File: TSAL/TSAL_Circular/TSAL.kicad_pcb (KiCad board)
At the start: 2 copper layers, 68.6 x 68.6 mm, 49 parts, among them J1 Main Connector, U1 L7805, U2 LM555, U3 SN754410

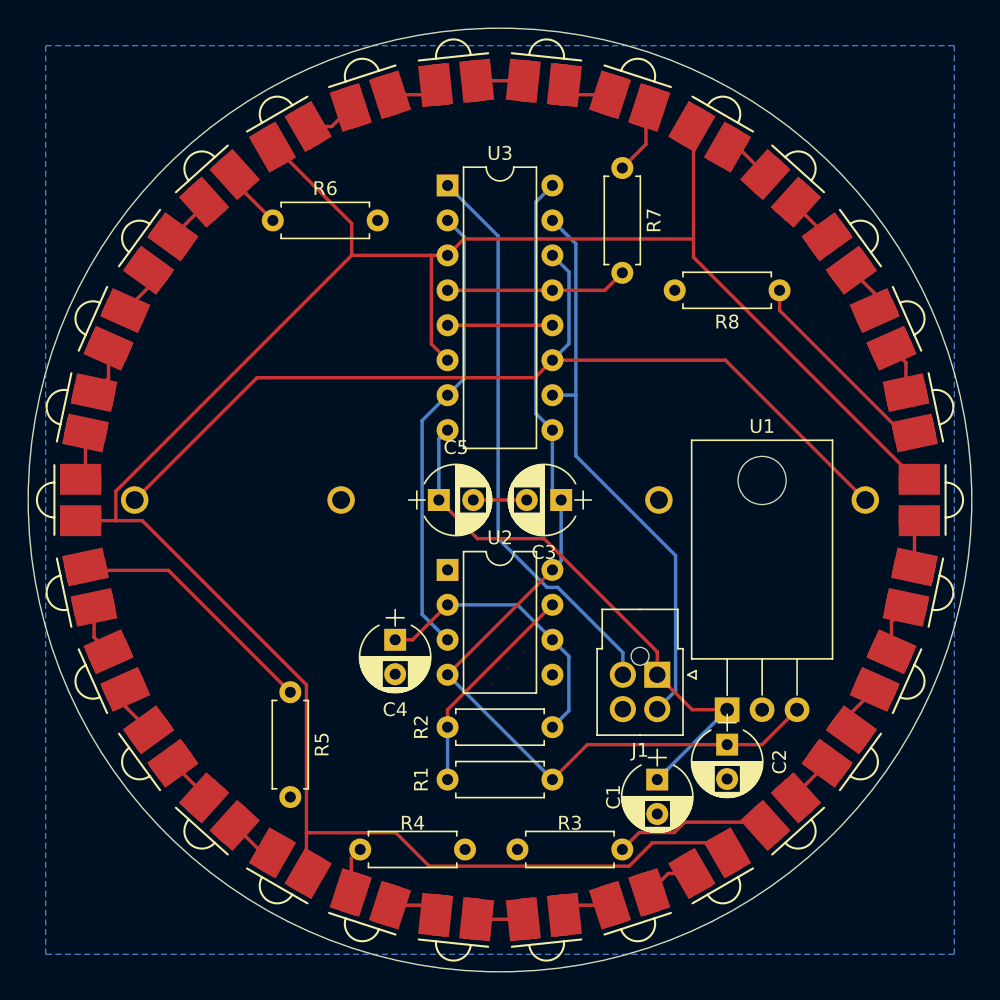
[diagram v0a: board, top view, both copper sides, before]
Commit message: add mounting holes and surface mount resistors to TSAL
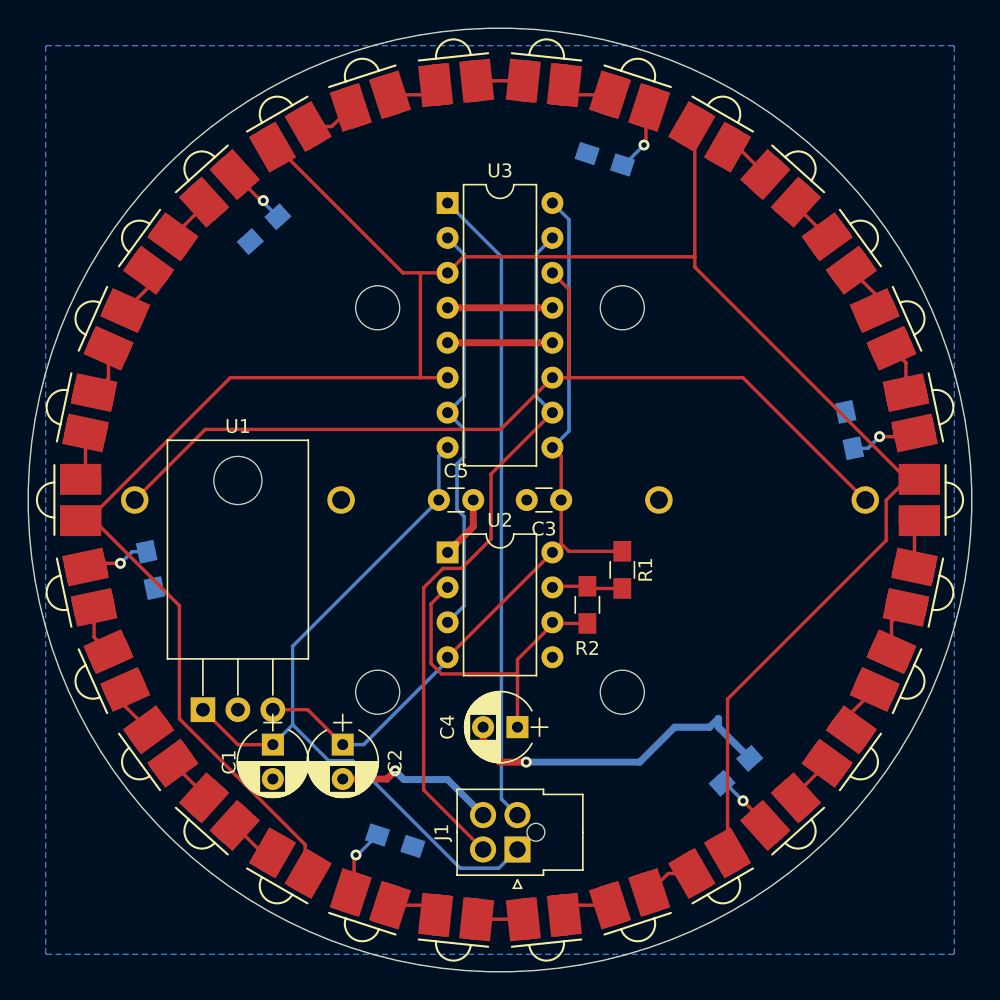
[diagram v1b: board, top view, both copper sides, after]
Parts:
- added H1: MtngHole, Mounting_Holes:MountingHole_3.2mm_M3, F.Cu at (143.5, 87.6)
- added H2: MtngHole, Mounting_Holes:MountingHole_3.2mm_M3, F.Cu at (143.5, 115.6)
- added H3: MtngHole, Mounting_Holes:MountingHole_3.2mm_M3, F.Cu at (161.3, 87.6)
- added H4: MtngHole, Mounting_Holes:MountingHole_3.2mm_M3, F.Cu at (161.3, 115.6)
- C3, C5: footprint Capacitors_THT:CP_Radial_D5.0mm_P2.50mm -> Capacitors_THT:C_Disc_D3.0mm_W1.6mm_P2.50mm
- R1, R2: footprint Resistors_THT:R_Axial_DIN0207_L6.3mm_D2.5mm_P7.62mm_Horizontal -> Resistors_SMD:R_0805_HandSoldering
- R3, R4, R5, R6, R7, R8: footprint Resistors_THT:R_Axial_DIN0207_L6.3mm_D2.5mm_P7.62mm_Horizontal -> Resistors_SMD:R_0805_HandSoldering; moved to B.Cu
- moved U1 38.1 mm to (130.8, 116.8)
- moved C1 28.1 mm to (135.9, 119.4)
- moved C2 27.9 mm to (141.0, 119.4)
- moved J1 16.3 mm to (153.7, 127.0), turned to 90 degrees
- moved R1 16.1 mm to (161.3, 106.7), turned to 270 degrees
- moved R2 13.5 mm to (158.8, 109.2), turned to 270 degrees
- moved R5 13.5 mm to (127.0, 106.7), turned to 282 degrees
- moved R8 11.4 mm to (177.8, 96.5), turned to 102 degrees
- moved C4 10.9 mm to (153.7, 118.1), turned to 180 degrees
- moved R3 10.0 mm to (169.5, 121.3), turned to 42 degrees
- moved R4 2.62 mm to (144.8, 126.4), turned to 342 degrees
- moved R7 1.42 mm to (160.0, 76.8), turned to 162 degrees
- moved U2 1.27 mm to (148.6, 105.4)
- moved U3 1.27 mm to (148.6, 80.0)
- moved R6 0.90 mm to (135.3, 81.9), turned to 222 degrees
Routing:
- net /GND: track 24.7 -> 55.7 mm, vias 0 -> 2
- net Net-(D15-Pad1): track 18.8 -> 5.15 mm, vias 0 -> 1
- net /12V: track 40.8 -> 54.2 mm
- net /5V: track 70.9 -> 58.9 mm
- net Net-(R1-Pad2): track 15.9 -> 5.18 mm
- net /SIG_RTDS: track 41.5 -> 51.9 mm
- net Net-(D30-Pad1): track 15.1 -> 5.15 mm, vias 0 -> 1
- net Net-(D5-Pad1): track 11.6 -> 4.70 mm, vias 0 -> 1
- net /SIG_TSAL: track 41.3 -> 46.6 mm
- net Net-(C4-Pad1): track 20.9 -> 23.8 mm
- net Net-(U2-Pad3): track 33.0 -> 30.3 mm
- net Net-(D10-Pad1): track 3.66 -> 5.26 mm, vias 0 -> 1
- net /RTDS_H: track 70.1 -> 68.6 mm
- net /OSC: track 171.5 -> 172.4 mm
- net Net-(D25-Pad1): track 5.42 -> 5.26 mm, vias 0 -> 1
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
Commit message: hopefully finalize PCBs for send to manufacturing
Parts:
- R3, R4, R5, R6, R7, R8: moved to F.Cu
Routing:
- net /GND: track 55.7 -> 35.7 mm, vias 2 -> 8
- net /RTDS_H: track 68.6 -> 77.3 mm
- net /SIG_TSAL: track 46.6 -> 50.8 mm
- net /SIG_RTDS: track 51.9 -> 48.7 mm
- net /OSC: track 172.4 -> 170.1 mm
- net /5V: track 58.9 -> 59.8 mm
- net /12V: track 54.2 -> 54.7 mm
- net Net-(D20-Pad1): track 4.73 -> 4.66 mm, vias 1 -> 0
- net Net-(D25-Pad1): track 5.26 -> 5.20 mm, vias 1 -> 0
- net Net-(D10-Pad1): track 5.26 -> 5.20 mm, vias 1 -> 0
- net Net-(D5-Pad1): track 4.70 -> 4.66 mm, vias 1 -> 0
- net Net-(D30-Pad1): vias 1 -> 0
- net Net-(D15-Pad1): vias 1 -> 0

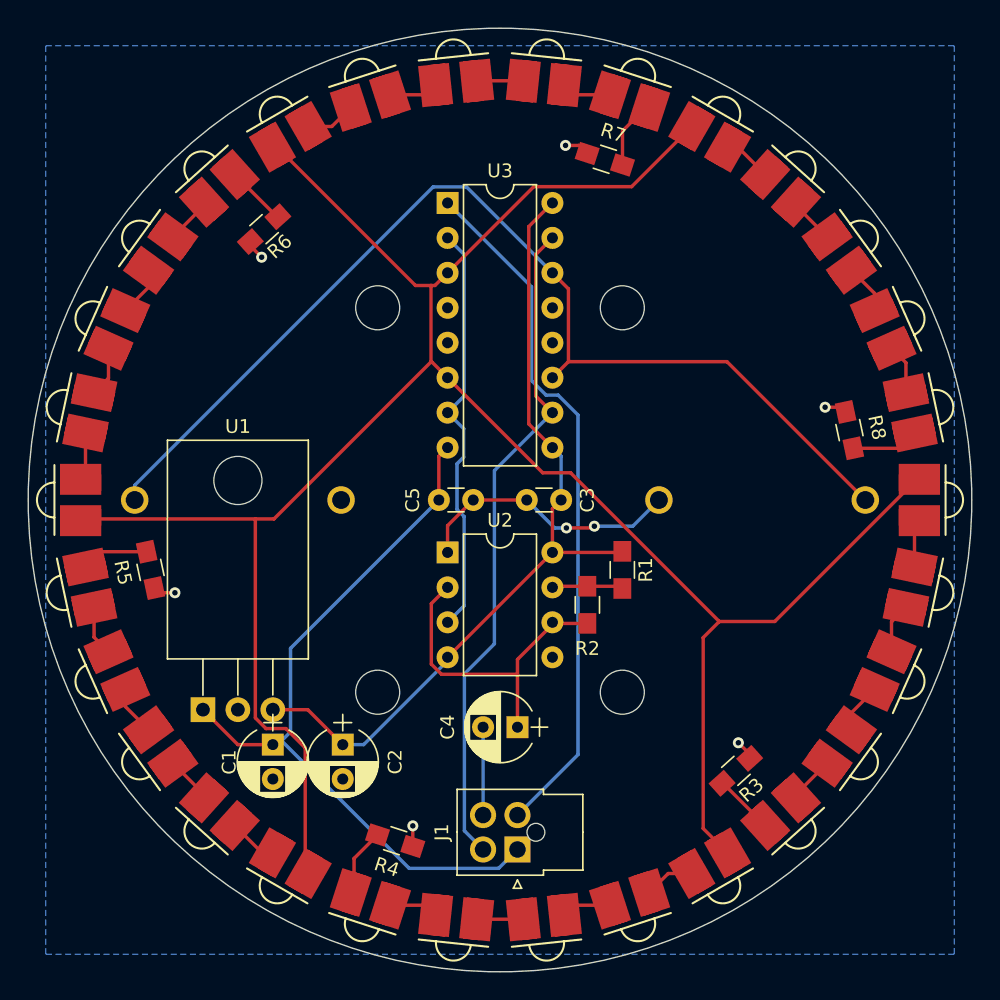
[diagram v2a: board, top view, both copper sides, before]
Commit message: Edit some component labels and other items for PCB send out
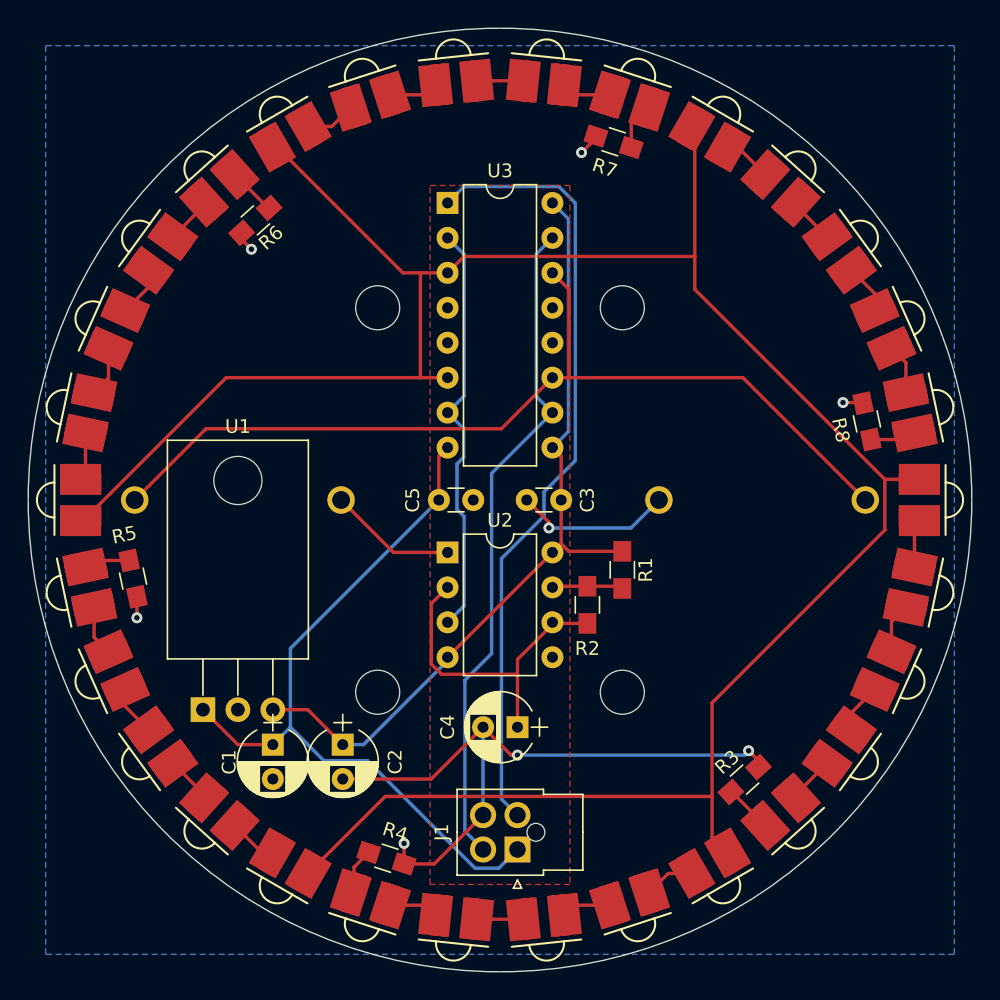
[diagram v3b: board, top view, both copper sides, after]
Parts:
- moved R4 1.42 mm to (144.1, 127.6)
- moved R5 1.42 mm to (125.7, 107.3)
- moved R7 1.42 mm to (160.7, 75.6)
- moved R8 1.42 mm to (179.1, 95.9)
- moved R3 0.90 mm to (170.2, 121.9)
- moved R6 0.90 mm to (134.6, 81.3)
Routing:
- net /GND: track 35.7 -> 75.6 mm
- net /RTDS_H: track 77.3 -> 68.6 mm
- net /SIG_TSAL: track 50.8 -> 57.5 mm
- net /OSC: track 170.1 -> 173.1 mm
- net Net-(D15-Pad1): track 5.15 -> 3.62 mm
- net Net-(D10-Pad1): track 5.20 -> 3.66 mm
- net Net-(D25-Pad1): track 5.20 -> 3.66 mm
- net Net-(D30-Pad1): track 5.15 -> 3.62 mm
- net Net-(D5-Pad1): track 4.66 -> 3.77 mm
- net Net-(D20-Pad1): track 4.66 -> 3.77 mm
- net /5V: track 59.8 -> 58.9 mm
- added copper zone on F.Cu, net /GND
